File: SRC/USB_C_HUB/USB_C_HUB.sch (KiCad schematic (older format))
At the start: 2 parts

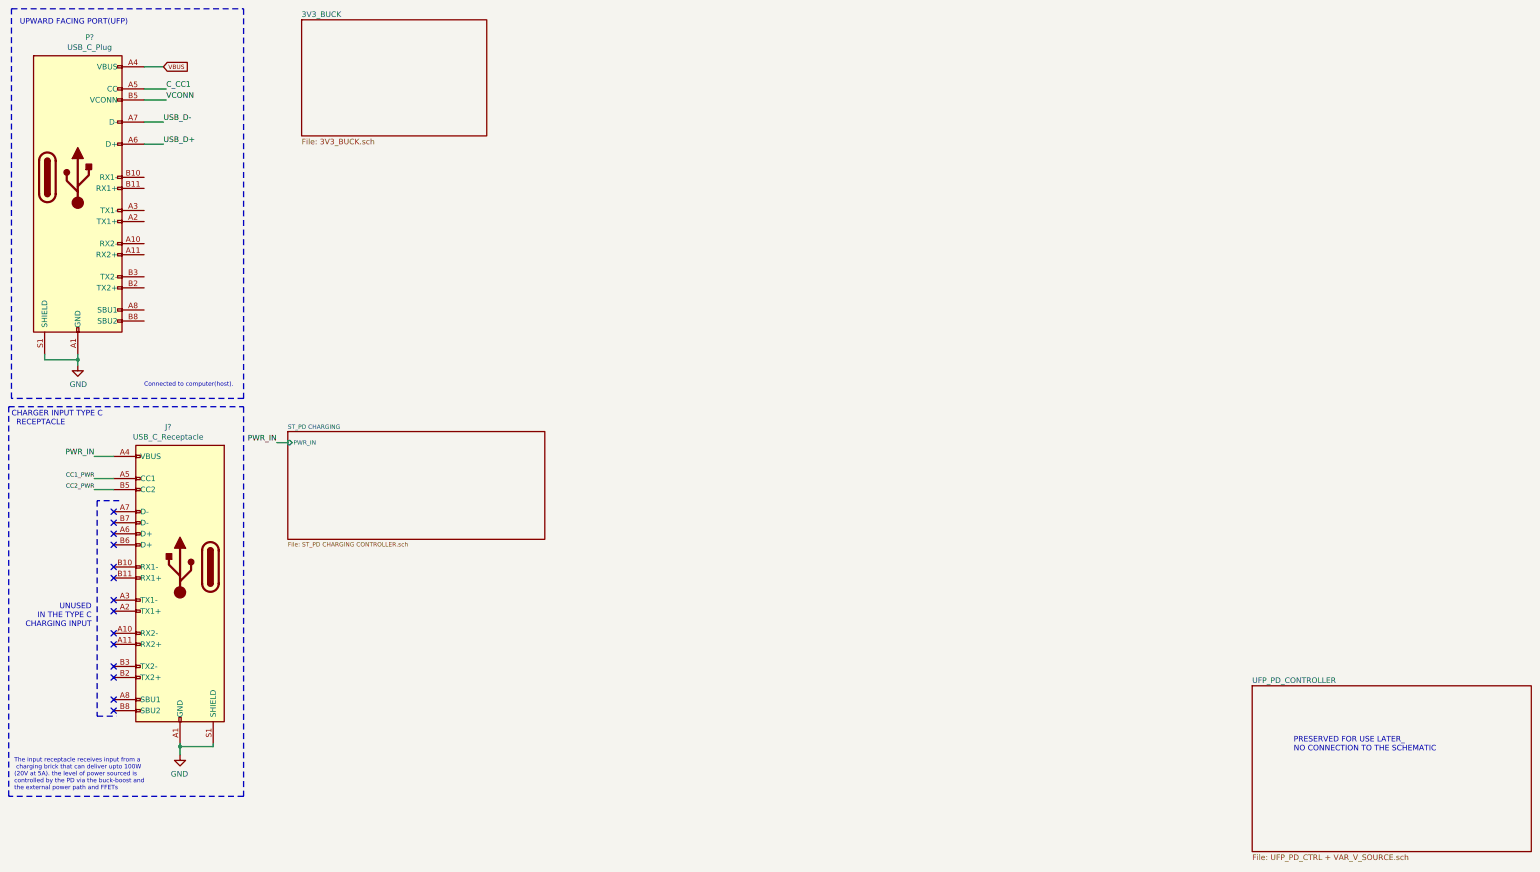
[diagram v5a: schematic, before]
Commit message: usb c mux
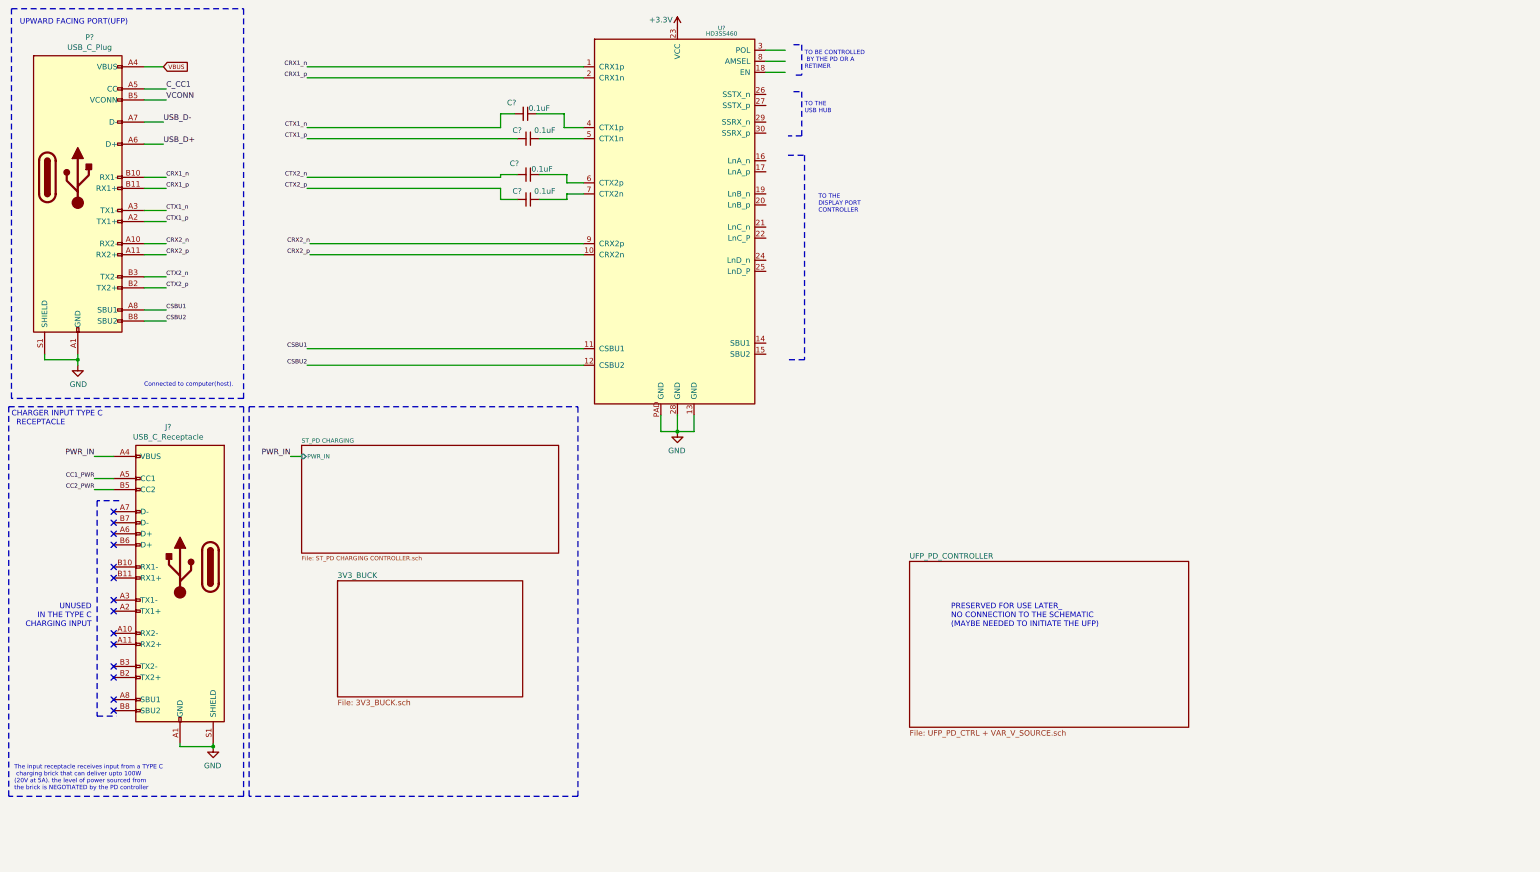
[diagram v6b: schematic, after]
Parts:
- added C? (x4): 0.1uF, symbol Device:C_Small
- added U?: HD3SS460, symbol usb_hub:HD3SS460
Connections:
- net labels added: +3.3V, CRX1_n, CRX1_p, CRX2_n, CRX2_p, CSBU1, CSBU2, CTX1_n, CTX1_p, CTX2_n, CTX2_p
- wire segments 17 -> 60
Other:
- note added: "PRESERVED FOR USE LATER_\nNO CONNECTION TO THE SCHEMATIC\n(MAYBE NEEDED TO INITIATE THE UFP)"
- note added: "TO BE CONTROLLED\n BY THE PD OR A\nRETIMER"
- note added: "TO THE \nDISPLAY PORT\nCONTROLLER"
- note added: "TO THE \nUSB HUB"
- note added: "The input receptacle receives input from a TYPE C\n charging brick that can deliver upto 100W\n(20V at 5A). the level of power sourced from\nthe brick is NEGOTIATED by the PD controller"
- note removed: "PRESERVED FOR USE LATER_\nNO CONNECTION TO THE SCHEMATIC"
- note removed: "The input receptacle receives input from a\n charging brick that can deliver upto 100W\n(20V at 5A). the level of power sourced is \ncontrolled by the PD via the buck-boost and \nthe external power path and FFETs"

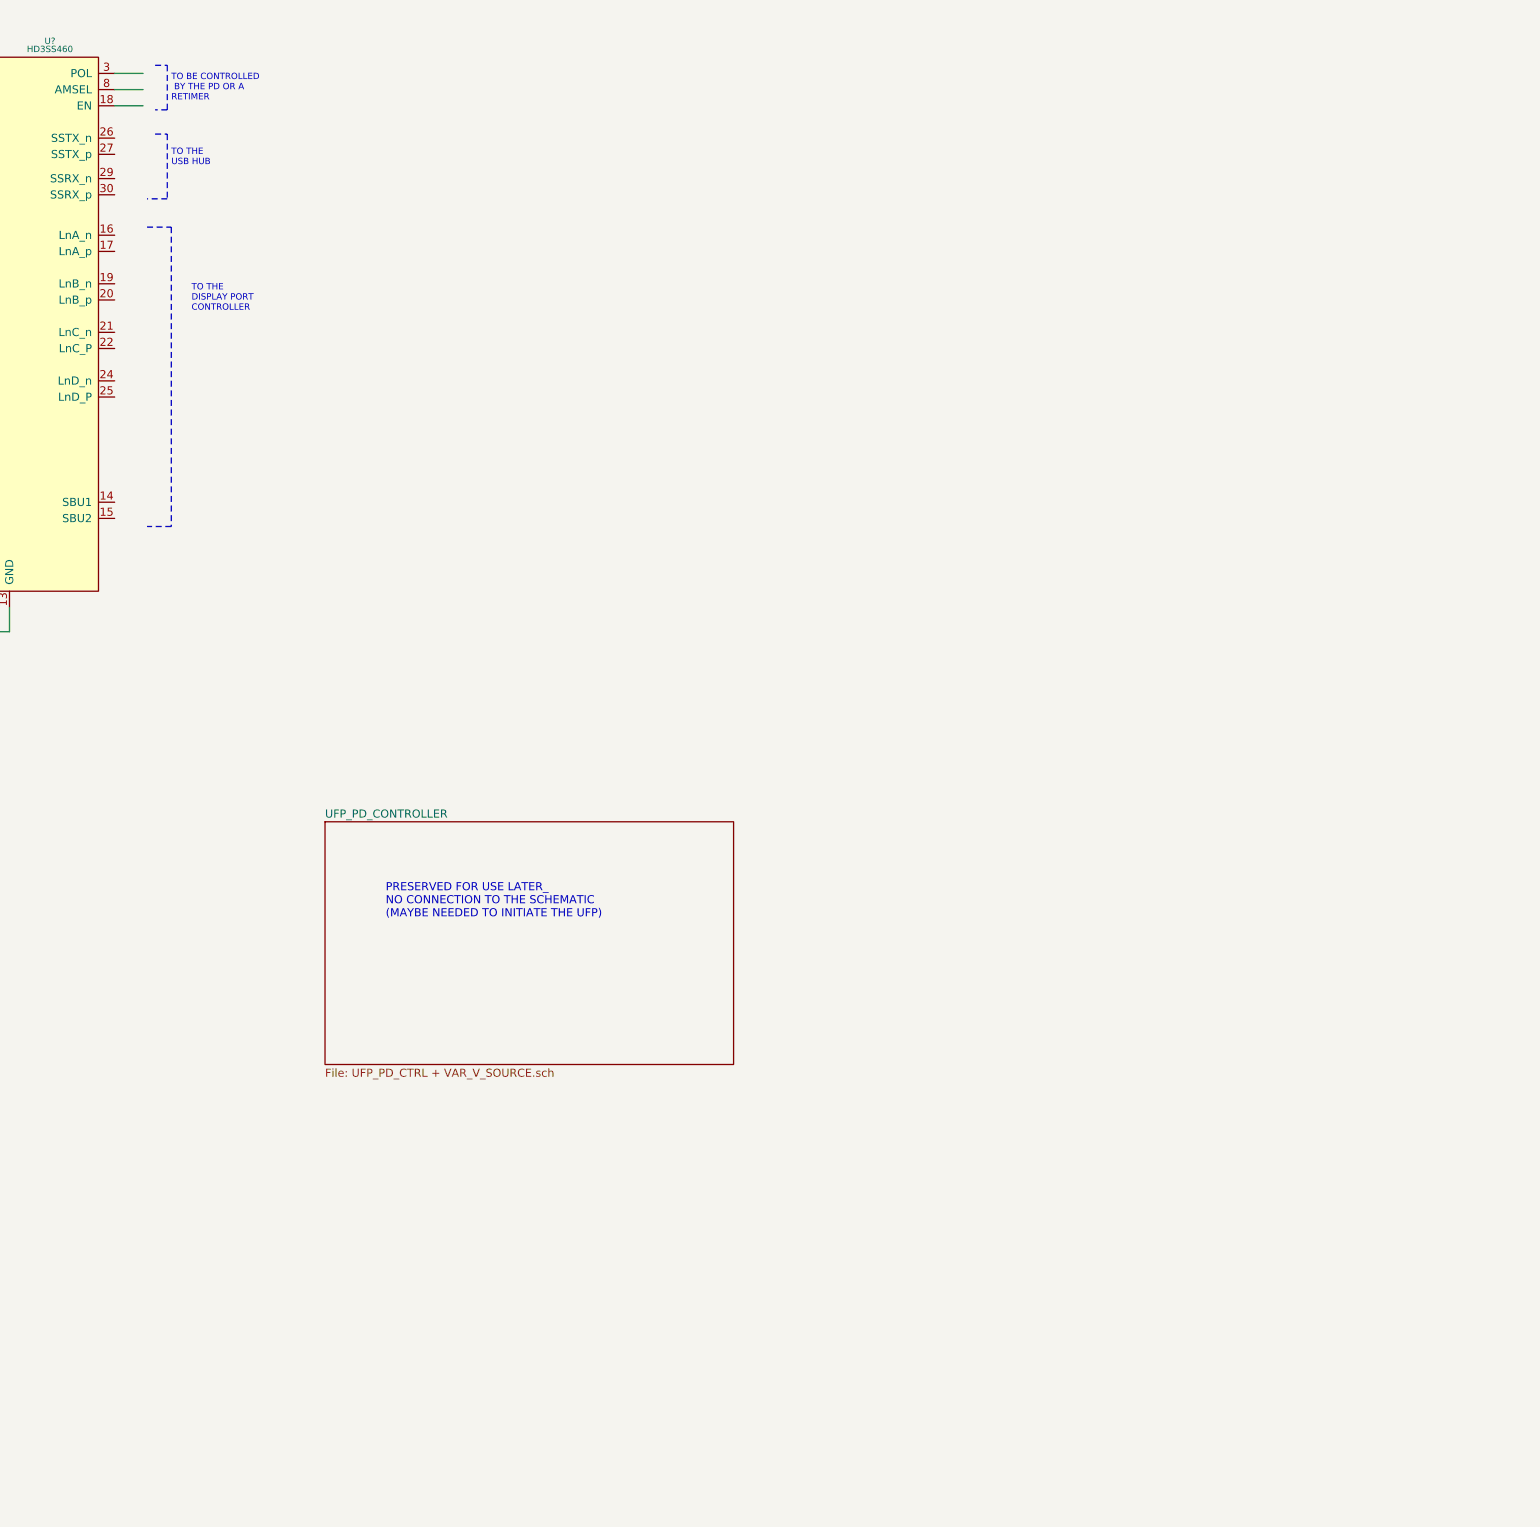
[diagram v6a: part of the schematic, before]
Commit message: usb MUX with DFPs
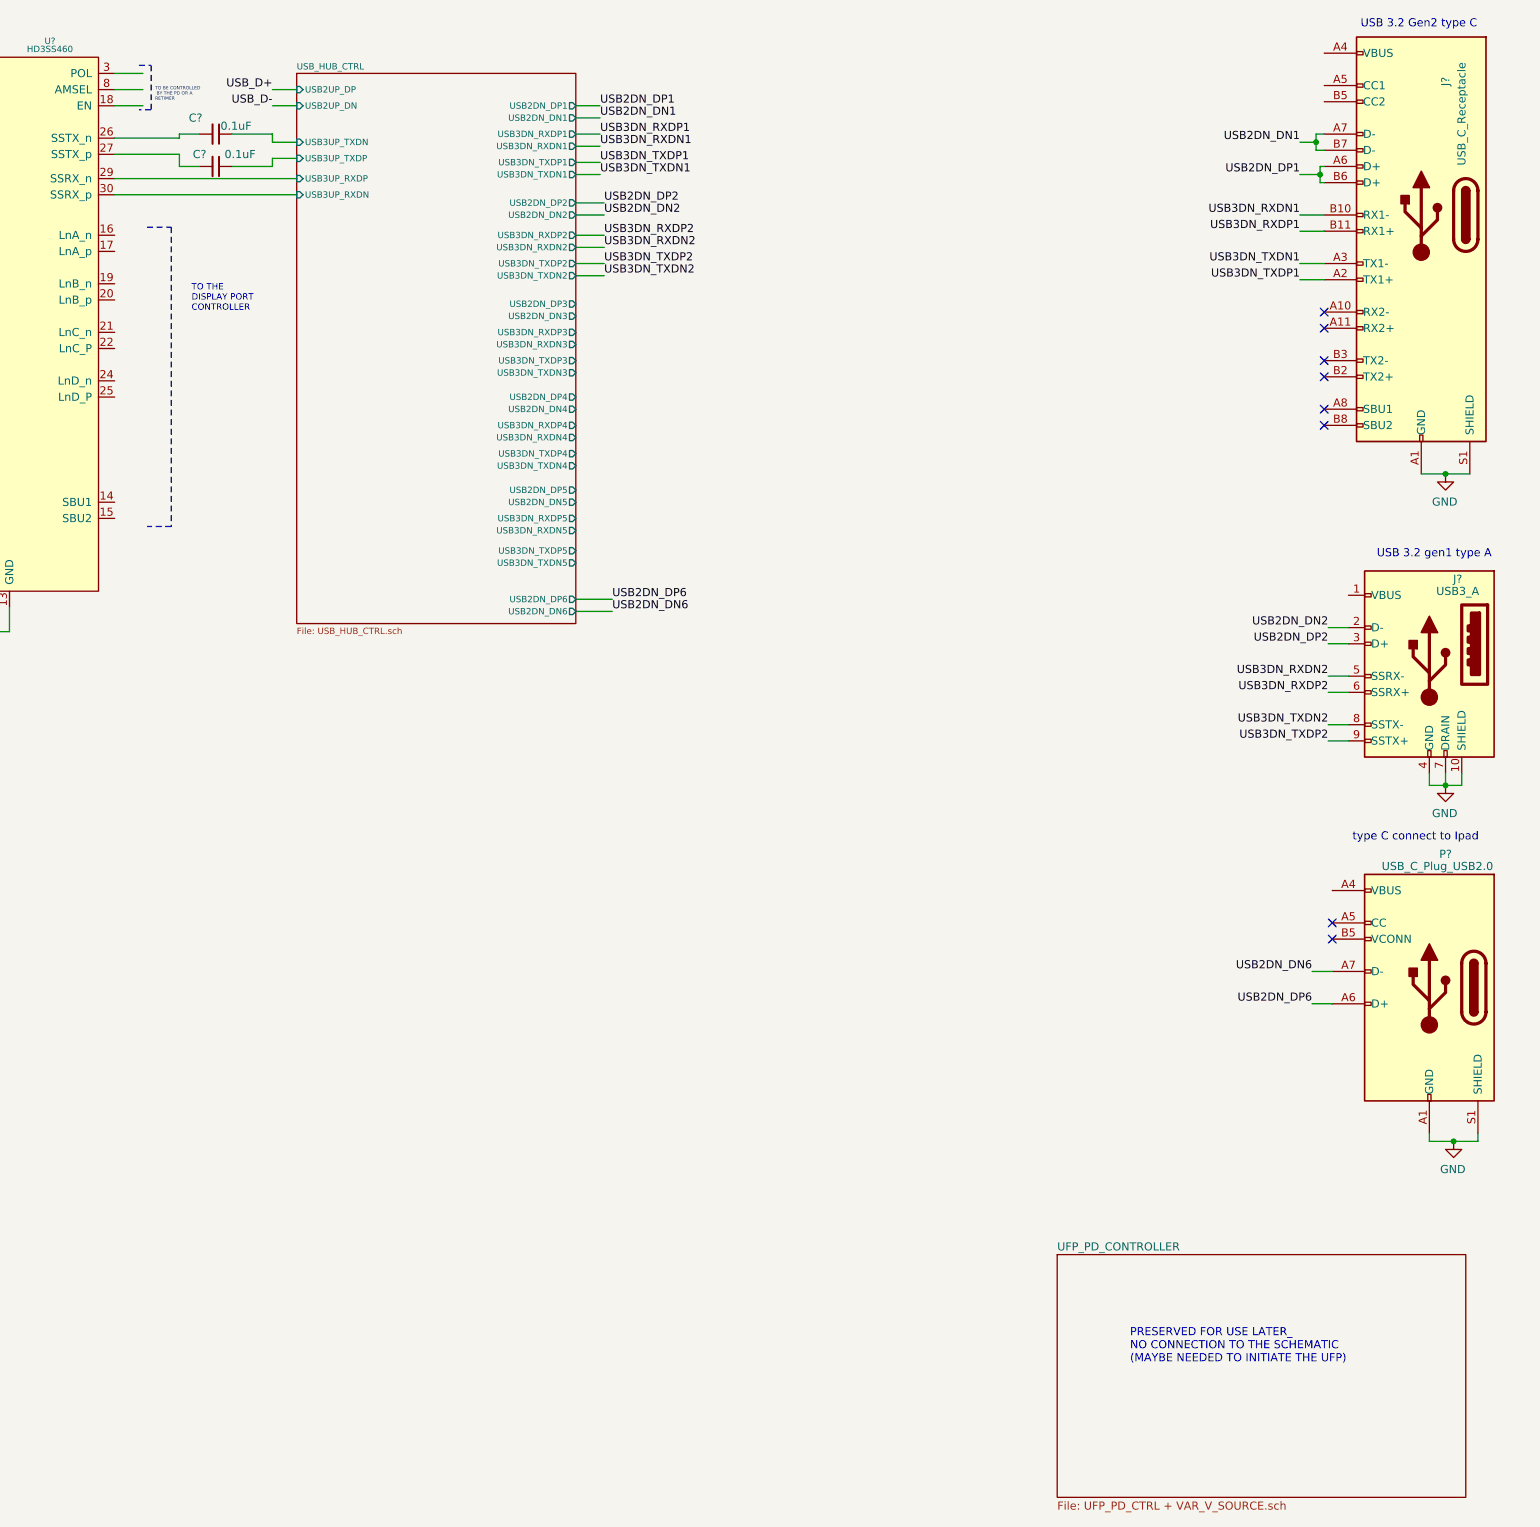
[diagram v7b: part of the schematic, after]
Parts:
- added C? (x2): 0.1uF, symbol Device:C_Small
- added J?: USB_C_Receptacle, symbol Connector:USB_C_Receptacle
- added J?: USB3_A, symbol Connector:USB3_A
- added P?: USB_C_Plug_USB2.0, symbol Connector:USB_C_Plug_USB2.0
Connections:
- net labels added: USB2DN_DN1, USB2DN_DN2, USB2DN_DN6, USB2DN_DP1, USB2DN_DP2, USB2DN_DP6, USB3DN_RXDN1, USB3DN_RXDN2, USB3DN_RXDP1, USB3DN_RXDP2, USB3DN_TXDN1, USB3DN_TXDN2, USB3DN_TXDP1, USB3DN_TXDP2
- wire segments 60 -> 123
- no-connect marks 14 -> 22
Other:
- note added: "USB 3.2 Gen2 type C"
- note added: "USB 3.2 gen1 type A"
- note added: "type C connect to Ipad"
- note removed: "TO THE \nUSB HUB"

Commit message: commit with all DFPs properly connected
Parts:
- added C?: 0.1uF, symbol Device:C_Small
- added R?: R_US, symbol Device:R_US
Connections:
- net GND: now also C?.1, R?.1; no longer P?.S1 (SHIELD)
- new net Earth_Clean: C?.2, P?.S1 (SHIELD), R?.2
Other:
- note added: "EHERNET df PORT"
- note added: "USB_CHASIS"
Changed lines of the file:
@@
 $Descr A3 16535 11693
 encoding utf-8
-Sheet 1 5
+Sheet 1 7
 Title ""
 Date ""
@@
 Text Notes 625  750  0    50   ~ 0
 UPWARD FACING PORT(UFP)\n
-$Comp
-L OLIMEX_Power:GND #PWR?
-U 1 1 6184FD01
-P 1150 3825
-F 0 "#PWR?" H 1150 3575 50  0001 C CNN
-F 1 "GND" H 1155 3652 50  0000 C CNN
-F 2 "" H 1150 3825 60  0000 C CNN
-F 3 "" H 1150 3825 60  0000 C CNN
-	1    1150 3825
-	1    0    0    -1
-$EndComp
 Wire Wire Line
 	1150 3725 1150 3775
@@
 	1750 1125 1925 1125
 Wire Notes Line
-	2650 600  2650 4125
-Wire Notes Line
-	2650 4125 550  4125
-Wire Notes Line
-	550  4125 550  600
+	2650 600  2650 4150
+Wire Notes Line
+	2650 4150 550  4150
+Wire Notes Line
+	550  4150 550  600
 Wire Notes Line
 	550  600  2650 600
@@
 Wire Wire Line
 	850  3725 850  3775
-Wire Wire Line
-	850  3775 1150 3775
-Connection ~ 1150 3775
-Wire Wire Line
-	1150 3775 1150 3825
 Text Notes 1750 4025 0    39   ~ 0
 Connected to computer(host).\n
@@
 PWR_IN
 $Sheet
-S 13200 8275 2525 1500
+S 825  9500 2525 1500
 U 61EF7DEC
 F0 "UFP_PD_CONTROLLER" 50
 F1 "UFP_PD_CTRL + VAR_V_SOURCE.sch" 50
 $EndSheet
-Text Notes 13650 8950 0    50   ~ 0
+Text Notes 1275 10175 0    50   ~ 0
   PRESERVED FOR USE LATER_\nNO CONNECTION TO THE SCHEMATIC\n(MAYBE NEEDED TO INITIATE THE UFP)
 Wire Wire Line
@@
 Wire Notes Line
 	5675 4200 5675 7725
-Wire Notes Line
-	5675 7725 2700 7725
 Wire Notes Line
 	2700 7725 2700 4200
@@
 	15800 7575 15650 7575
 Connection ~ 15650 7575
+Wire Notes Line
+	5675 7725 2700 7725
+$Sheet
+S 12825 1150 925  1150
+U 631C6BCF
+F0 "ETHERNET" 50
+F1 "LAN7850 ETHERNET.sch" 50
+F2 "USB_DP" O L 12825 1250 39
+F3 "USB_DM" O L 12825 1375 39
+$EndSheet
+$Comp
+L Device:C_Small C?
+U 1 1 632ABF2E
+P 1000 3950
+F 0 "C?" V 950 3875 50  0000 C CNN
+F 1 "0.1uF" V 950 4075 50  0000 C CNN
+F 2 "" H 1000 3950 50  0001 C CNN
+F 3 "~" H 1000 3950 50  0001 C CNN
+	1    1000 3950
+	0    1    1    0
+$EndComp
+$Comp
+L Device:R_US R?
+U 1 1 632B4A9A
+P 1000 3775
+F 0 "R?" V 795 3775 50  0000 C CNN
+F 1 "R_US" V 886 3775 50  0000 C CNN
+F 2 "" V 1040 3765 50  0001 C CNN
+F 3 "~" H 1000 3775 50  0001 C CNN
+	1    1000 3775
+	0    1    1    0
+$EndComp
+Wire Wire Line
+	850  3775 850  3950
+Wire Wire Line
+	850  3950 900  3950
+Connection ~ 850  3775
+Connection ~ 1150 3775
+Wire Wire Line
+	1150 3950 1150 3775
+Wire Wire Line
+	1100 3950 1150 3950
+$Comp
+L OLIMEX_Power:GND #PWR?
+U 1 1 6184FD01
+P 1325 3900
+F 0 "#PWR?" H 1325 3650 50  0001 C CNN
+F 1 "GND" H 1330 3727 50  0000 C CNN
+F 2 "" H 1325 3900 60  0000 C CNN
+F 3 "" H 1325 3900 60  0000 C CNN
+	1    1325 3900
+	1    0    0    -1
+$EndComp
+Wire Wire Line
+	1325 3900 1325 3775
+Wire Wire Line
+	1325 3775 1150 3775
+$Comp
+L power:Earth_Clean #PWR?
+U 1 1 632DC3BF
+P 700 3875
+AR Path="/632DC3BF" Ref="#PWR?"  Part="1"
+AR Path="/631C6BCF/632DC3BF" Ref="#PWR?"  Part="1"
+F 0 "#PWR?" H 950 3875 50  0001 C CNN
+F 1 "Earth_Clean" H 1000 3725 50  0001 C CNN
+F 2 "" H 700 3825 50  0001 C CNN
+F 3 "~" H 700 3825 50  0001 C CNN
+	1    700  3875
+	1    0    0    -1
+$EndComp
+Wire Wire Line
+	850  3775 700  3775
+Wire Wire Line
+	700  3775 700  3875
+Text Notes 575  4100 0    39   ~ 0
+USB_CHASIS
+Text Label 10400 2400 0    50   ~ 0
+USB2DN_DP3
+Text Label 10400 2475 0    50   ~ 0
+USB2DN_DN3
+Wire Wire Line
+	10225 2400 10400 2400
+Wire Wire Line
+	10225 2475 10400 2475
+Text Label 12675 1250 2    50   ~ 0
+USB2DN_DP3
+Text Label 12675 1375 2    50   ~ 0
+USB2DN_DN3
+Wire Wire Line
+	12825 1250 12675 1250
+Wire Wire Line
+	12825 1375 12675 1375
+Text Notes 12850 1050 0    50   ~ 0
+EHERNET df PORT
+$Sheet
+S 12850 2700 1250 925
+U 63D2BAD4
+F0 "SD CARD UHS" 31
+F1 "SD_CARD UHS II.sch" 31
+F2 "USB+" O L 12850 2800 39
+F3 "USB-" O L 12850 2925 39
+$EndSheet
+Text Label 10425 2975 0    50   ~ 0
+USB2DN_DP4
+Text Label 10425 3050 0    50   ~ 0
+USB2DN_DN4
+Wire Wire Line
+	10225 2975 10425 2975
+Wire Wire Line
+	10225 3050 10425 3050
+Text Label 12675 2800 2    50   ~ 0
+USB2DN_DP4
+Text Label 12675 2925 2    50   ~ 0
+USB2DN_DN4
+Wire Wire Line
+	12850 2925 12675 2925
+Wire Wire Line
+	12675 2800 12850 2800
 $EndSCHEMATC
